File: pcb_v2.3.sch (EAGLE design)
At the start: 53 parts, among them J1 PJ301_THONKICONN6, J2 PJ301_THONKICONN6, J3 PJ301_THONKICONN6, J4 PJ301_THONKICONN6, U1 MCP6004, U2 TL074_SMD, U5 TL074

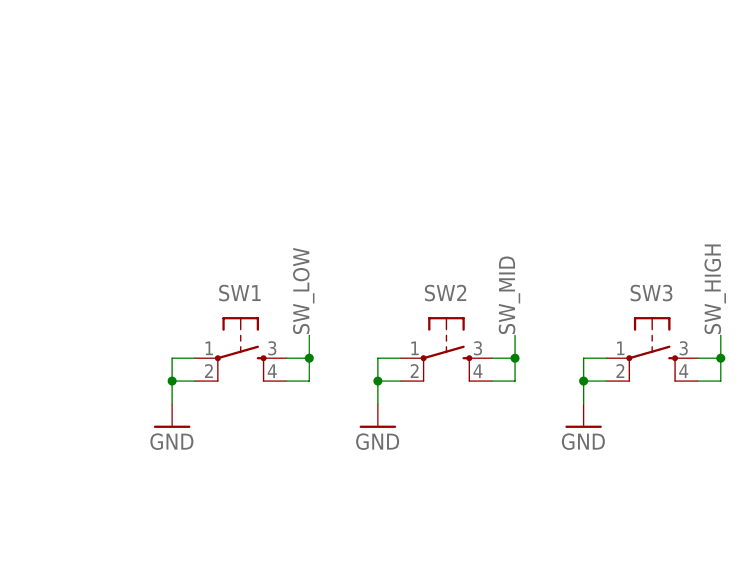
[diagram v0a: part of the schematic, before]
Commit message: fix switch ordering
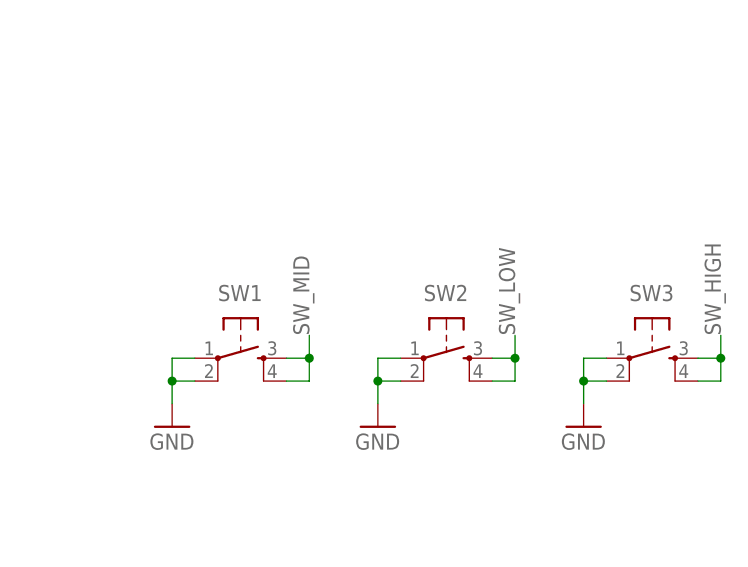
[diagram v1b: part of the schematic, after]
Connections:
- net SW_LOW: now also SW2.3, SW2.4; no longer SW1.3, SW1.4
- net SW_MID: now also SW1.3, SW1.4; no longer SW2.3, SW2.4
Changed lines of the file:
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@@
 <setting verticaltext="up"/>
 </settings>
-<grid distance="10" unitdist="mil" unit="mil" style="lines" multiple="1" display="no" altdistance="0.01" altunitdist="inch" altunit="inch"/>
+<grid distance="0.1" unitdist="inch" unit="inch" style="lines" multiple="1" display="no" altdistance="0.01" altunitdist="inch" altunit="inch"/>
 <layers>
 <layer number="1" name="Top" color="4" fill="1" visible="no" active="no"/>
@@
 <net name="SW_LOW" class="0">
 <segment>
+<pinref part="SV2" gate="G$1" pin="8"/>
+<wire x1="72.39" y1="161.29" x2="62.23" y2="161.29" width="0.1524" layer="91"/>
+<label x="63.5" y="161.29" size="1.778" layer="95"/>
+</segment>
+<segment>
+<wire x1="219.71" y1="148.59" x2="222.25" y2="148.59" width="0.1524" layer="91"/>
+<wire x1="222.25" y1="148.59" x2="222.25" y2="151.13" width="0.1524" layer="91"/>
+<wire x1="222.25" y1="151.13" x2="222.25" y2="153.67" width="0.1524" layer="91"/>
+<wire x1="219.71" y1="151.13" x2="222.25" y2="151.13" width="0.1524" layer="91"/>
+<junction x="222.25" y="151.13"/>
+<label x="222.25" y="153.67" size="1.778" layer="95" rot="R90"/>
+<pinref part="SW2" gate="S" pin="4"/>
+<pinref part="SW2" gate="S" pin="3"/>
+</segment>
+</net>
+<net name="SW_MID" class="0">
+<segment>
+<pinref part="SV2" gate="G$1" pin="6"/>
+<wire x1="72.39" y1="158.75" x2="62.23" y2="158.75" width="0.1524" layer="91"/>
+<label x="63.5" y="158.75" size="1.778" layer="95"/>
+</segment>
+<segment>
 <wire x1="196.85" y1="148.59" x2="199.39" y2="148.59" width="0.1524" layer="91"/>
 <wire x1="199.39" y1="148.59" x2="199.39" y2="151.13" width="0.1524" layer="91"/>
@@
 <pinref part="SW1" gate="S" pin="3"/>
 </segment>
-<segment>
-<pinref part="SV2" gate="G$1" pin="8"/>
-<wire x1="72.39" y1="161.29" x2="62.23" y2="161.29" width="0.1524" layer="91"/>
-<label x="63.5" y="161.29" size="1.778" layer="95"/>
-</segment>
-</net>
-<net name="SW_MID" class="0">
-<segment>
-<wire x1="219.71" y1="148.59" x2="222.25" y2="148.59" width="0.1524" layer="91"/>
-<wire x1="222.25" y1="148.59" x2="222.25" y2="151.13" width="0.1524" layer="91"/>
-<wire x1="222.25" y1="151.13" x2="222.25" y2="153.67" width="0.1524" layer="91"/>
-<wire x1="219.71" y1="151.13" x2="222.25" y2="151.13" width="0.1524" layer="91"/>
-<junction x="222.25" y="151.13"/>
-<label x="222.25" y="153.67" size="1.778" layer="95" rot="R90"/>
-<pinref part="SW2" gate="S" pin="4"/>
-<pinref part="SW2" gate="S" pin="3"/>
-</segment>
-<segment>
-<pinref part="SV2" gate="G$1" pin="6"/>
-<wire x1="72.39" y1="158.75" x2="62.23" y2="158.75" width="0.1524" layer="91"/>
-<label x="63.5" y="158.75" size="1.778" layer="95"/>
-</segment>
-</net>
+</net>
